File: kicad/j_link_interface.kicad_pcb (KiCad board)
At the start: 4 copper layers, 22.8 x 30.4 mm, 7 parts, among them J1 Conn_01x05_Pin, J2 SFH11-PBPC-D10-RA-BK, J3 FTSH-107-01-X-DV-K

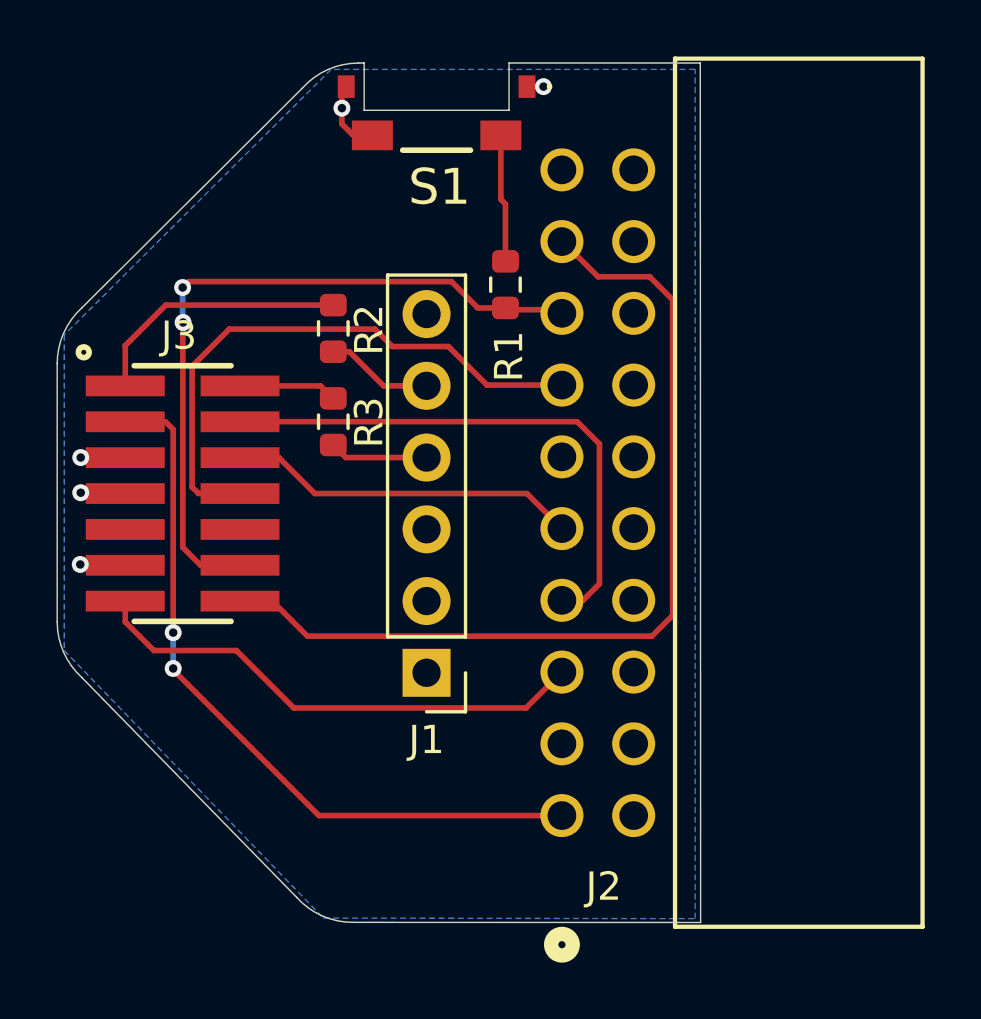
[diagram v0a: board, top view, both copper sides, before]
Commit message: Added some extra text. Increased PCB size. Fixed connector 3D position.
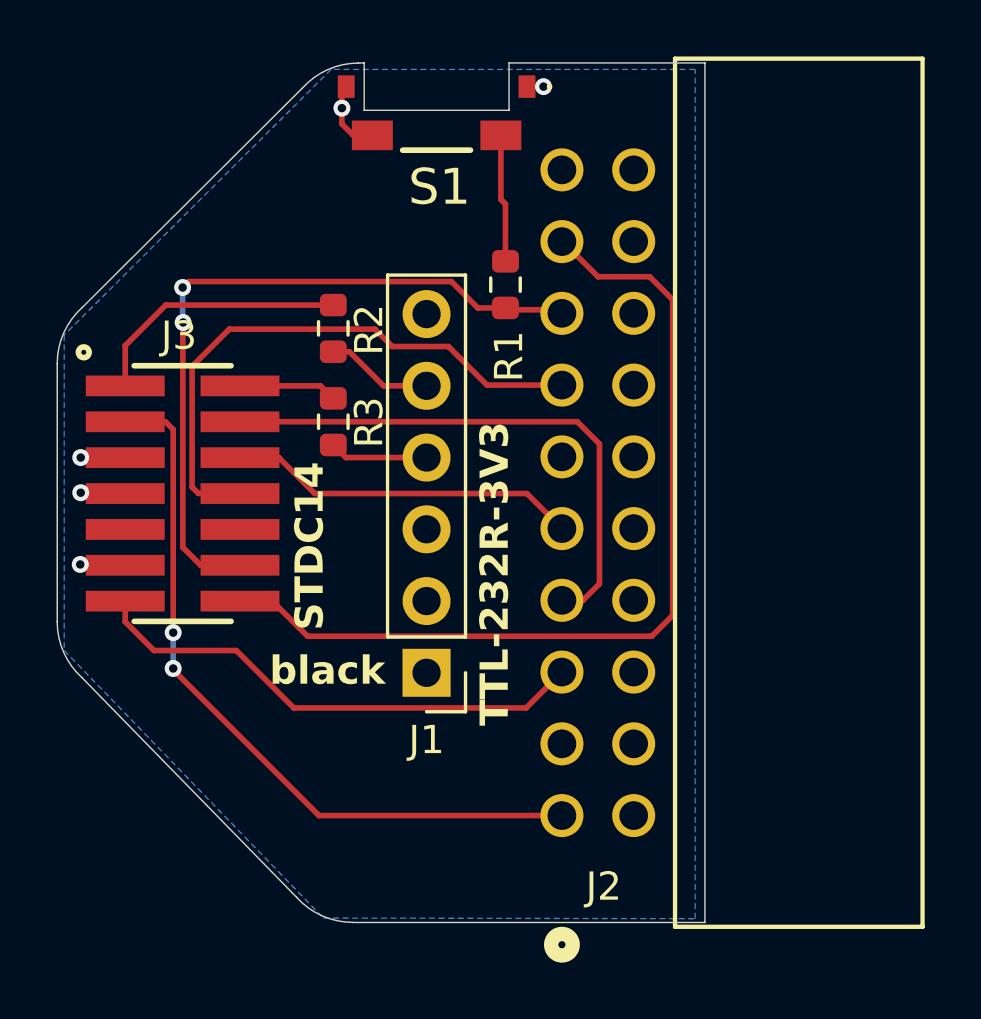
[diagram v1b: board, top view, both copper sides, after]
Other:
- board size 22.8 x 30.4 mm -> 22.9 x 30.4 mm
- board text added: "STDC14"
- board text added: "TTL-232R-3V3"
- board text added: "black"
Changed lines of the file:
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@@
 			)
 		)
-		(property "SupplierPN" "EVQ-P42B3MD"
+		(property "SupplierPN" "P15502CT-ND"
 			(at 0 0 180)
 			(unlocked yes)
@@
 		(sheetname "/")
 		(sheetfile "j_link_interface.kicad_sch")
-		(units
-			(unit
-				(name "A")
-				(pins "1" "3" "5" "7" "9" "11" "13" "15" "17" "19" "2" "4" "6" "8" "10"
-					"12" "14" "16" "18" "20"
-				)
-			)
-		)
 		(attr through_hole)
 		(duplicate_pad_numbers_are_jumpers no)
@@
 		(model "${KIPRJMOD}/local_library.3dshapes/SFH11-PBPC-D10-RA-BK.step"
 			(offset
-				(xyz 22.85 -12.5 3)
+				(xyz 22.85 -12.6 3)
 			)
 			(scale
@@
 	(gr_line
 		(start 122.428 60.3504)
-		(end 129.197083 60.3504)
+		(end 129.3622 60.3504)
 		(stroke
 			(width 0.05)
@@
 	)
 	(gr_line
-		(start 129.197083 60.3504)
-		(end 129.209811 90.7796)
+		(start 129.3622 60.3504)
+		(end 129.3622 90.7796)
 		(stroke
 			(width 0.05)
-			(type default)
+			(type solid)
 		)
 		(layer "Edge.Cuts")
 	)
 	(gr_line
-		(start 129.2098 90.7796)
-		(end 116.890766 90.775097)
+		(start 129.3622 90.7796)
+		(end 116.890766 90.7796)
 		(stroke
 			(width 0.05)
-			(type default)
+			(type solid)
 		)
 		(layer "Edge.Cuts")
 	)
+	(gr_text "black\n"
+		(at 113.9444 82.4484 0)
+		(layer "F.SilkS")
+		(effects
+			(font
+				(size 1 1)
+				(thickness 0.25)
+				(bold yes)
+			)
+			(justify left bottom)
+		)
+	)
+	(gr_text "STDC14"
+		(at 115.951 80.4418 90)
+		(layer "F.SilkS")
+		(effects
+			(font
+				(size 1 1)
+				(thickness 0.25)
+				(bold yes)
+			)
+			(justify left bottom)
+		)
+	)
+	(gr_text "TTL-232R-3V3"
+		(at 122.5042 83.82 90)
+		(layer "F.SilkS")
+		(effects
+			(font
+				(size 1 1)
+				(thickness 0.25)
+				(bold yes)
+			)
+			(justify left bottom)
+		)
+	)
 	(gr_text "j-link interface - ${REVISION}"
-		(at 121.793 84.074 270)
+		(at 121.3152 84.074 270)
 		(layer "B.SilkS")
 		(effects
